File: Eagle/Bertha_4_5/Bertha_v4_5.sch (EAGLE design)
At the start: 136 parts, among them CON1 JACK_DC_BARREL, CON2 JACK_DC_BARREL, IC1 MCP1703DB, IC4 DRV8811, J1 RJ12RIGHTANGLE-I2C, J2 RJ12RIGHTANGLE-I2C, Q5 BSP75, Q6 BSP75, U1 HX711, U100 RN2483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

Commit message: All connectors on the connector slot
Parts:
- removed JP1: (no value), freetronics-master-v1:M04SCREW
- added JP3: (no value), jumper:JP4E
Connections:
- net N$10: now also JP3.2; no longer JP1.3
- net N$4: now also JP3.4; no longer JP1.1
- net N$55: now also JP3.1; no longer JP1.4
- net N$56: now also JP3.3; no longer JP1.2
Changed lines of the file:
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@@
 <part name="C35" library="freetronics-master-v1" deviceset="CAP" device="0805" value="220nF"/>
 <part name="R38" library="rcl" deviceset="R-EU_" device="R2010" value="0.2R 1W"/>
-<part name="JP1" library="freetronics-master-v1" deviceset="M04" device="SCREW"/>
 <part name="C47" library="freetronics-original" deviceset="CAP_POL" device="E" value="100uF 50V"/>
 <part name="P+38" library="SparkFun" deviceset="3.3V" device=""/>
@@
 <part name="P+50" library="SparkFun" deviceset="3.3V" device=""/>
 <part name="P+62" library="SparkFun" deviceset="3.3V" device=""/>
+<part name="JP3" library="jumper" deviceset="JP4E" device=""/>
 </parts>
 <sheets>
@@
 <attribute name="VALUE" x="706.12" y="17.78" size="1.27" layer="96"/>
 </instance>
-<instance part="JP1" gate="G$1" x="708.66" y="45.72" rot="MR0"/>
 <instance part="C47" gate="G$1" x="731.52" y="76.2" smashed="yes">
 <attribute name="NAME" x="732.663" y="76.6826" size="1.778" layer="95"/>
@@
 <instance part="P+50" gate="G$1" x="645.16" y="86.36"/>
 <instance part="P+62" gate="G$1" x="739.14" y="27.94"/>
+<instance part="JP3" gate="G$1" x="706.12" y="48.26" rot="R270"/>
 </instances>
 <busses>
@@
 <wire x1="685.8" y1="40.64" x2="690.88" y2="40.64" width="0.1524" layer="91"/>
 <wire x1="690.88" y1="40.64" x2="690.88" y2="43.18" width="0.1524" layer="91"/>
-<pinref part="JP1" gate="G$1" pin="1"/>
 <wire x1="690.88" y1="43.18" x2="703.58" y2="43.18" width="0.1524" layer="91"/>
+<pinref part="JP3" gate="G$1" pin="4"/>
 </segment>
 </net>
@@
 <wire x1="688.34" y1="50.8" x2="685.8" y2="50.8" width="0.1524" layer="91"/>
 <wire x1="688.34" y1="50.8" x2="688.34" y2="48.26" width="0.1524" layer="91"/>
-<pinref part="JP1" gate="G$1" pin="3"/>
 <wire x1="688.34" y1="48.26" x2="703.58" y2="48.26" width="0.1524" layer="91"/>
+<pinref part="JP3" gate="G$1" pin="2"/>
 </segment>
 </net>
@@
 <wire x1="685.8" y1="53.34" x2="690.88" y2="53.34" width="0.1524" layer="91"/>
 <wire x1="690.88" y1="53.34" x2="690.88" y2="50.8" width="0.1524" layer="91"/>
-<pinref part="JP1" gate="G$1" pin="4"/>
 <wire x1="690.88" y1="50.8" x2="703.58" y2="50.8" width="0.1524" layer="91"/>
+<pinref part="JP3" gate="G$1" pin="1"/>
 </segment>
 </net>
@@
 <wire x1="688.34" y1="43.18" x2="685.8" y2="43.18" width="0.1524" layer="91"/>
 <wire x1="688.34" y1="43.18" x2="688.34" y2="45.72" width="0.1524" layer="91"/>
-<pinref part="JP1" gate="G$1" pin="2"/>
 <wire x1="688.34" y1="45.72" x2="703.58" y2="45.72" width="0.1524" layer="91"/>
+<pinref part="JP3" gate="G$1" pin="3"/>
 </segment>
 </net>

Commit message: Bertha V4.5 with DRV8811, still need to put the connectors closer to the edge ref #47
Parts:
- removed LDM1, LDM4: RED, adafruit:LEDCHIP-LED0805
- removed RK11, RK8: 10K, rcl:R-EU_R0805
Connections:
- removed net D3: IC4.DIR
- removed net D6: IC4.STEP
- removed net N$31: LDM4.C, RK8.2
- removed net N$37: LDM1.C, RK11.2
- net +12V: no longer LDM1.A, LDM4.A
- net D8*: now also IC4.DIR
- net D9*: now also IC4.STEP
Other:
- note removed: "0603"
- note removed: "Stepper 2"
- moved on the sheet: C25, C26, C27, C28, C29, C30, C31, C32, C33, C34, C35, C47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

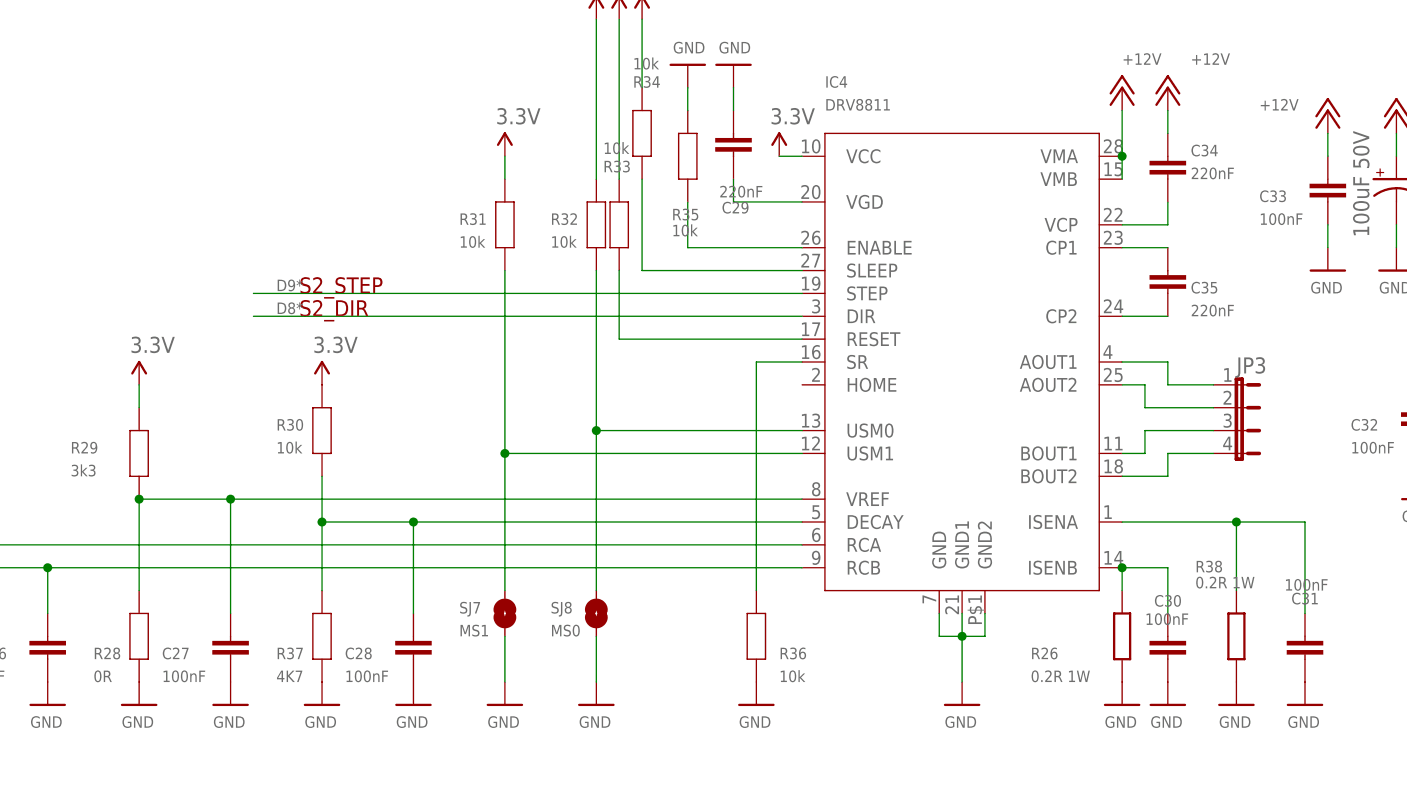
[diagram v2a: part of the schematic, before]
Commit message: silk screen correction, need to optimize the current limiting resistors on 4.5
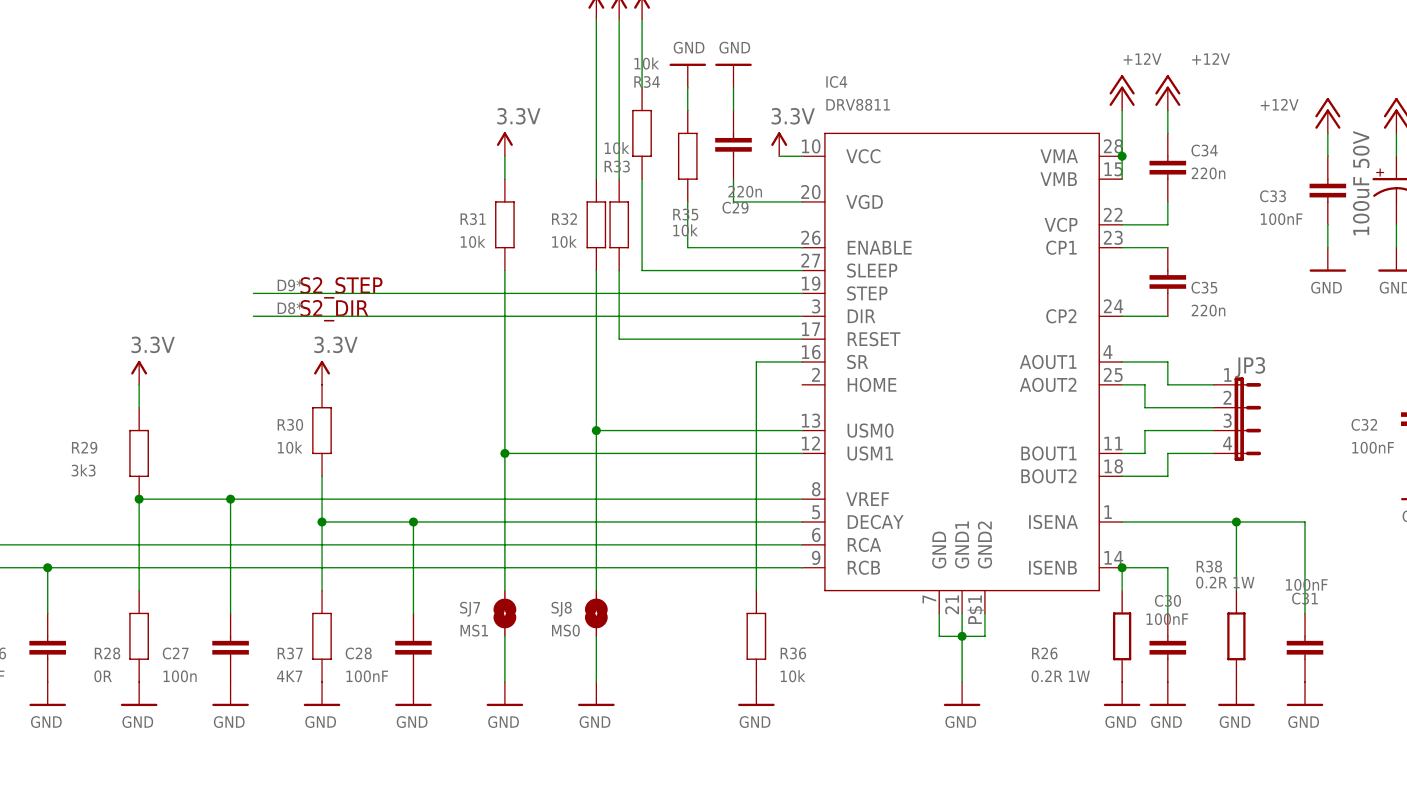
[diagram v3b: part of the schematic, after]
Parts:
- C27: value 100nF -> 100n
- C29, C34, C35: value 220nF -> 220n
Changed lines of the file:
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@@
 <part name="C26" library="freetronics-master-v1" deviceset="CAP" device="0805" value="1nF"/>
 <part name="R28" library="freetronics-master-v1" deviceset="RESISTOR" device="0805" value="0R"/>
-<part name="C27" library="freetronics-master-v1" deviceset="CAP" device="0805" value="100nF"/>
+<part name="C27" library="freetronics-master-v1" deviceset="CAP" device="0805" value="100n"/>
 <part name="R29" library="freetronics-master-v1" deviceset="RESISTOR" device="0805" value="3k3"/>
 <part name="R30" library="freetronics-master-v1" deviceset="RESISTOR" device="0805" value="10k"/>
@@
 <part name="R34" library="freetronics-master-v1" deviceset="RESISTOR" device="0805" value="10k"/>
 <part name="C28" library="freetronics-master-v1" deviceset="CAP" device="0805" value="100nF"/>
-<part name="C29" library="freetronics-master-v1" deviceset="CAP" device="0805" value="220nF"/>
+<part name="C29" library="freetronics-master-v1" deviceset="CAP" device="0805" value="220n"/>
 <part name="R35" library="freetronics-master-v1" deviceset="RESISTOR" device="0805" value="10k"/>
 <part name="R36" library="freetronics-master-v1" deviceset="RESISTOR" device="0805" value="10k"/>
@@
 <part name="C32" library="freetronics-master-v1" deviceset="CAP" device="0805" value="100nF"/>
 <part name="C33" library="freetronics-master-v1" deviceset="CAP" device="0805" value="100nF"/>
-<part name="C34" library="freetronics-master-v1" deviceset="CAP" device="0805" value="220nF"/>
-<part name="C35" library="freetronics-master-v1" deviceset="CAP" device="0805" value="220nF"/>
+<part name="C34" library="freetronics-master-v1" deviceset="CAP" device="0805" value="220n"/>
+<part name="C35" library="freetronics-master-v1" deviceset="CAP" device="0805" value="220n"/>
 <part name="R38" library="rcl" deviceset="R-EU_" device="R2010" value="0.2R 1W"/>
 <part name="C47" library="freetronics-original" deviceset="CAP_POL" device="E" value="100uF 50V"/>

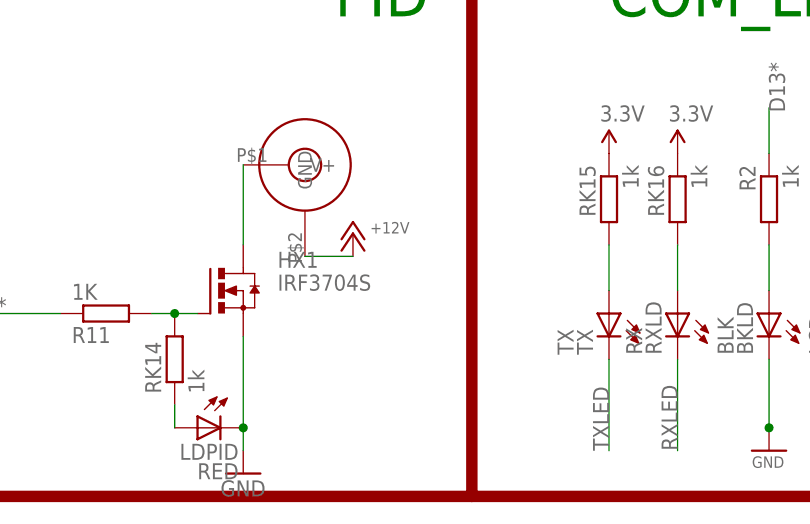
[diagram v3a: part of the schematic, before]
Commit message: changed PID FET part, ref #72
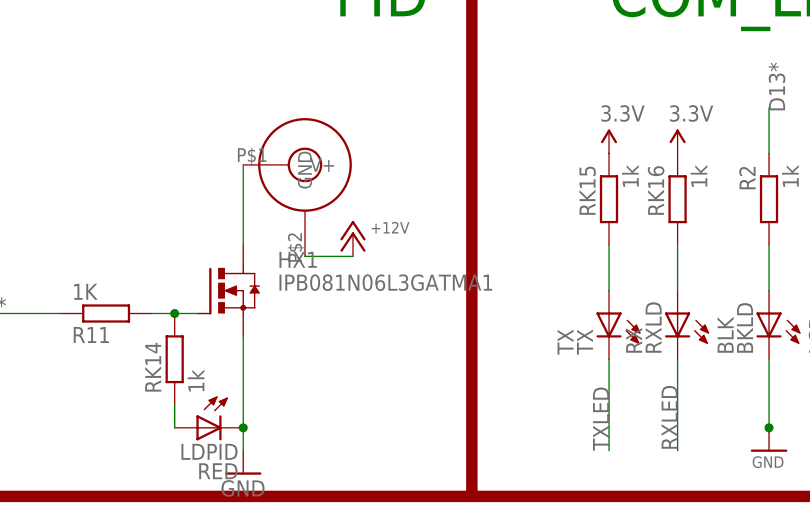
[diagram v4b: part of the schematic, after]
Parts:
- HX1: value IRF3704S -> IPB081N06L3GATMA1
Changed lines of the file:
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@@
 <?xml version="1.0" encoding="utf-8"?>
 <!DOCTYPE eagle SYSTEM "eagle.dtd">
-<eagle version="6.5.0">
+<eagle version="7.5.0">
 <drawing>
 <settings>
@@
 <part name="GND8" library="supply1" deviceset="GND" device=""/>
 <part name="GND27" library="supply1" deviceset="GND" device=""/>
-<part name="HX1" library="transistor-power" deviceset="IRF3704" device="S"/>
+<part name="HX1" library="transistor-power" deviceset="IRF3704" device="S" value="IPB081N06L3GATMA1"/>
 <part name="R11" library="rcl" deviceset="R-EU_" device="R0805" value="1K"/>
 <part name="P+2" library="supply1" deviceset="+12V" device=""/>
